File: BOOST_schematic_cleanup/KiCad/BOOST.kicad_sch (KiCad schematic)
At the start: 290 parts, among them J1 Conn_01x01_Pin, J10 Conn_02x15_2.54mm, J11 Conn_02x15_2.54mm, J2 Conn_01x01_Pin, J3 Conn_01x01_Pin, J4 Conn_01x01_Pin, J5 Conn_01x01_Pin, J6 Conn_01x01_Pin, J7 Conn_01x01_Pin, J8 Conn_01x01_Pin, J9 Conn_01x11, M1 HYG180N10, M10 HYG180N10, M2 HYG180N10, M3 HYG180N10, M4 HYG180N10, M5 HYG180N10, M6 HYG180N10, M7 HYG180N10, M8 HYG180N10, M9 HYG180N10, Q1 PNP, U1 L78L05_SOT89, U10 UCC21520DW, U101 74HC00, U102 74HC00, U103 74HC00, U104 74HC14, U105 74HC14, U106 CD74HC4066, U11 MCP6241, U12 MCP6241, U13 MCP6241, U14 MCP6561, U15 UCC21520DW, U16 LM2940_12, U17 L78L05_SOT89, U18 4017, U19 UCC21520DW, U2 MCP6561, U21 MCP6561, U22 MCP6241, U23 MCP6241, U24 MCP6241, U25 INA241A4xD, U26 MCP4451-103E/ST, U28 74HC4051, U3 MCP6241, U4 MCP6561, U5 MCP6561, U6 MCP6241, U7 MCP6241, U8 UCC21520DW

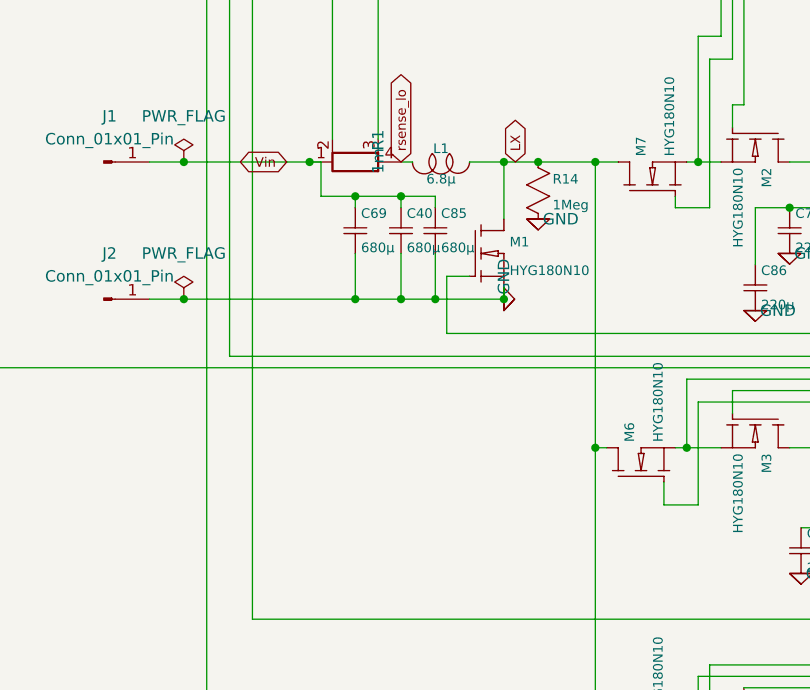
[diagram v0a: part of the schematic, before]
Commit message: added diodes from input to output
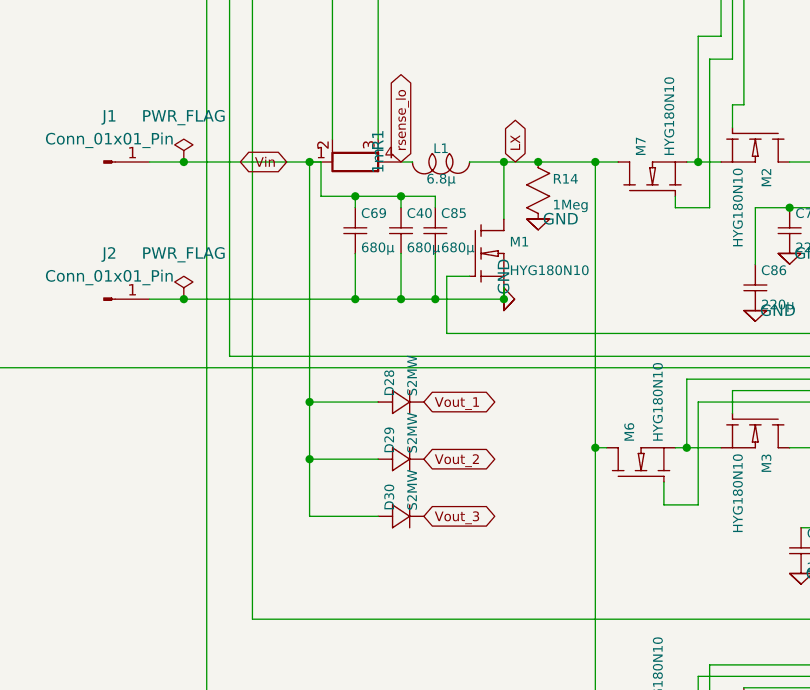
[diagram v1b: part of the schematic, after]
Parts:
- added D28, D29, D30: S2MW, Diode_SMD:D_SOD-123F, symbol ltspice:diode
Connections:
- net Vin: now also D28.2 (+), D29.2 (+), D30.2 (+)
- net Vout_1: now also D28.1 (-)
- net Vout_2: now also D29.1 (-)
- net Vout_3: now also D30.1 (-)

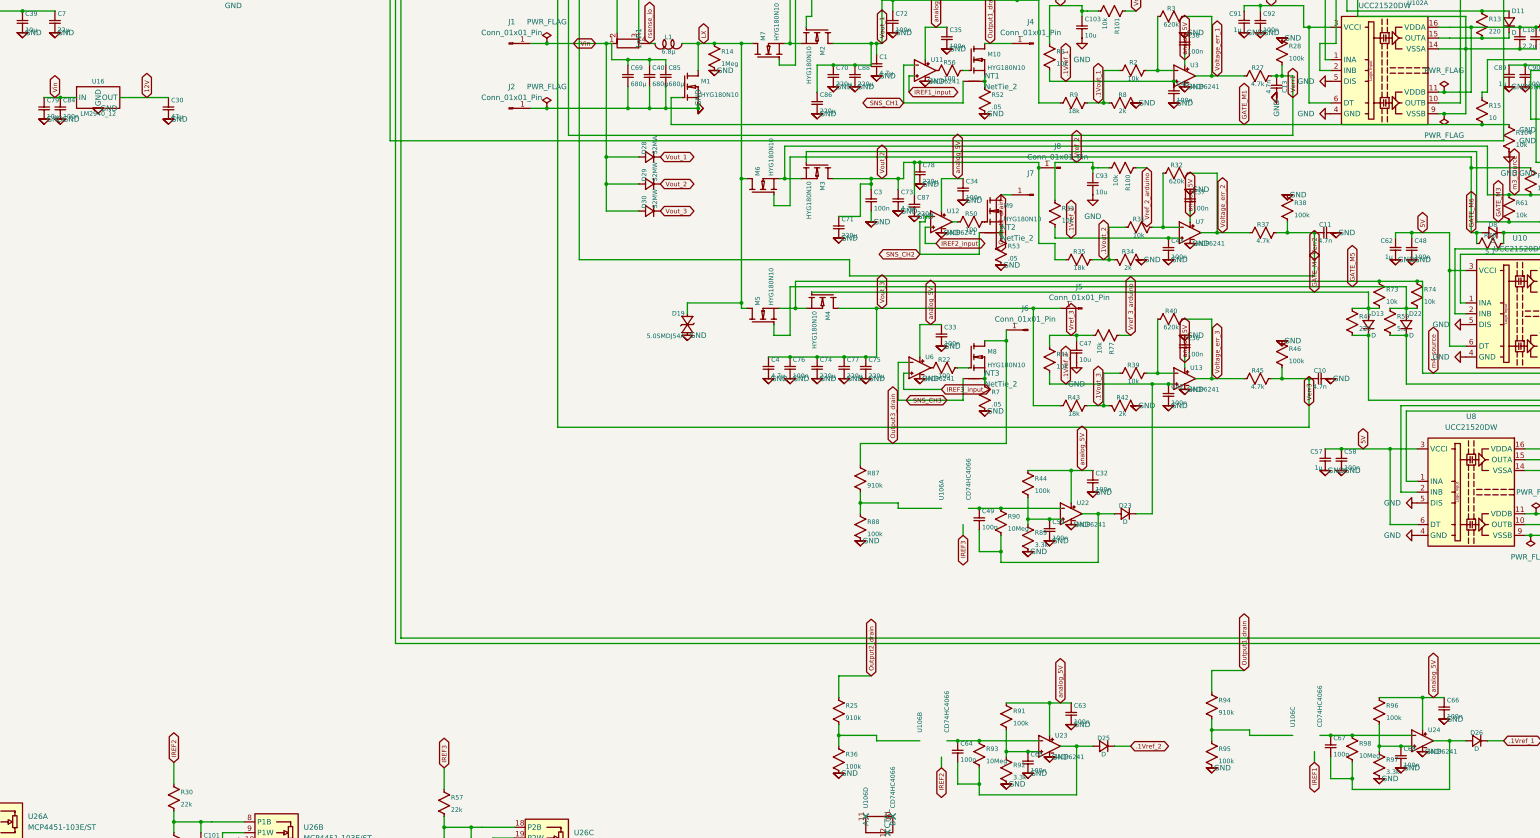
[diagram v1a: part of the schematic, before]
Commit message: changed power board to 6 layers
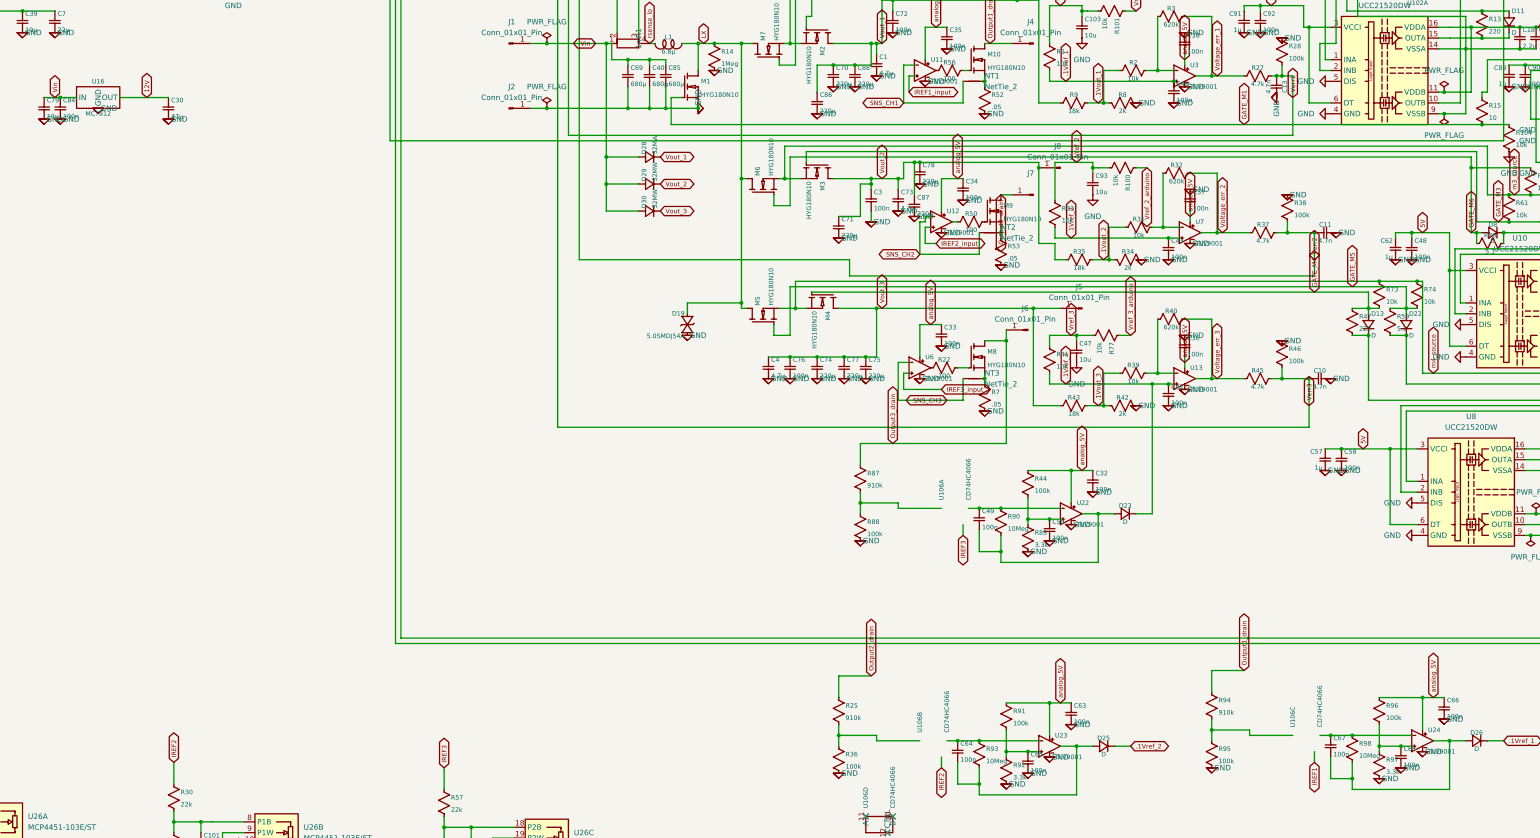
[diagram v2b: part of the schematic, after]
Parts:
- C70, C71, C75, C77, C78, C88: MPN EEH-ZU1H221P -> EEH-ZS1H221P
- U11, U12, U13, U22, U23, U24, U3, U6, U7: value MCP6241 -> TLV9001; MPN (none) -> TLV9001IDBVR
- U16: value LM2940_12 -> MC7812; MPN (none) -> MC7812BD2TR4G
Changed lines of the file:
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@@
 			)
 		)
-		(property "Value" "MCP6241"
+		(property "Value" "TLV9001"
 			(at 335.28 181.61 0)
 			(show_name no)
@@
 			)
 		)
-		(property "Sim.Library" "C:\\Users\\bubba\\AppData\\Local\\LTspice\\lib\\sub\\MCP6241.lib"
+		(property "Sim.Library" "../LTspice/TLV9001.lib"
 			(at 334.01 173.99 0)
 			(hide yes)
@@
 			)
 		)
+		(property "MPN" "TLV9001IDBVR"
+			(at 334.01 173.99 0)
+			(hide yes)
+			(show_name no)
+			(do_not_autoplace no)
+			(effects
+				(font
+					(size 1.27 1.27)
+				)
+			)
+		)
 		(pin "4"
 		)
@@
 			)
 		)
-		(property "MPN" "EEH-ZU1H221P"
+		(property "MPN" "EEH-ZS1H221P"
 			(at 248.92 139.7 0)
 			(hide yes)
@@
 			)
 		)
-		(property "MPN" "EEH-ZU1H221P"
+		(property "MPN" "EEH-ZS1H221P"
 			(at 256.54 208.28 0)
 			(hide yes)
@@
 			)
 		)
-		(property "Value" "MCP6241"
+		(property "Value" "TLV9001"
 			(at 273.05 143.51 0)
 			(show_name no)
@@
 			)
 		)
-		(property "Sim.Library" "C:\\Users\\bubba\\AppData\\Local\\LTspice\\lib\\sub\\MCP6241.lib"
+		(property "Sim.Library" "../LTspice/TLV9001.lib"
 			(at 271.78 135.89 0)
 			(hide yes)
@@
 			)
 		)
+		(property "MPN" "TLV9001IDBVR"
+			(at 271.78 135.89 0)
+			(hide yes)
+			(show_name no)
+			(do_not_autoplace no)
+			(effects
+				(font
+					(size 1.27 1.27)
+				)
+			)
+		)
 		(pin "3"
 		)
@@
 			)
 		)
-		(property "Value" "MCP6241"
+		(property "Value" "TLV9001"
 			(at 389.89 300.99 0)
 			(show_name no)
@@
 			)
 		)
-		(property "Sim.Library" "C:\\Users\\bubba\\AppData\\Local\\LTspice\\lib\\sub\\MCP6241.lib"
+		(property "Sim.Library" "../LTspice/TLV9001.lib"
 			(at 388.62 293.37 0)
 			(hide yes)
@@
 			)
 		)
+		(property "MPN" "TLV9001IDBVR"
+			(at 388.62 293.37 0)
+			(hide yes)
+			(show_name no)
+			(do_not_autoplace no)
+			(effects
+				(font
+					(size 1.27 1.27)
+				)
+			)
+		)
 		(pin "2"
 		)
@@
 			)
 		)
-		(property "Value" "MCP6241"
+		(property "Value" "TLV9001"
 			(at 271.78 213.36 0)
 			(show_name no)
@@
 			)
 		)
-		(property "Sim.Library" "C:\\Users\\bubba\\AppData\\Local\\LTspice\\lib\\sub\\MCP6241.lib"
+		(property "Sim.Library" "../LTspice/TLV9001.lib"
 			(at 270.51 205.74 0)
 			(hide yes)
@@
 			)
 		)
+		(property "MPN" "TLV9001IDBVR"
+			(at 270.51 205.74 0)
+			(hide yes)
+			(show_name no)
+			(do_not_autoplace no)
+			(effects
+				(font
+					(size 1.27 1.27)
+				)
+			)
+		)
 		(pin "2"
 		)
@@
 			)
 		)
-		(property "MPN" "EEH-ZU1H221P"
+		(property "MPN" "EEH-ZS1H221P"
 			(at 254 139.7 0)
 			(hide yes)
@@
 			)
 		)
-		(property "MPN" "EEH-ZU1H221P"
+		(property "MPN" "EEH-ZS1H221P"
 			(at 251.46 208.28 0)
 			(hide yes)
@@
 			)
 		)
-		(property "MPN" "EEH-ZU1H221P"
+		(property "MPN" "EEH-ZS1H221P"
 			(at 269.24 162.56 0)
 			(hide yes)
@@
 			)
 		)
-		(property "Value" "MCP6241"
+		(property "Value" "TLV9001"
 			(at 302.26 302.26 0)
 			(show_name no)
@@
 			)
 		)
-		(property "Sim.Library" "C:\\Users\\bubba\\AppData\\Local\\LTspice\\lib\\sub\\MCP6241.lib"
+		(property "Sim.Library" "../LTspice/TLV9001.lib"
 			(at 300.99 294.64 0)
 			(hide yes)
@@
 			)
 		)
+		(property "MPN" "TLV9001IDBVR"
+			(at 300.99 294.64 0)
+			(hide yes)
+			(show_name no)
+			(do_not_autoplace no)
+			(effects
+				(font
+					(size 1.27 1.27)
+				)
+			)
+		)
 		(pin "3"
 		)
@@
 			)
 		)
-		(property "Value" "MCP6241"
+		(property "Value" "TLV9001"
 			(at 334.01 215.9 0)
 			(show_name no)
@@
 			)
 		)
-		(property "Sim.Library" "C:\\Users\\bubba\\AppData\\Local\\LTspice\\lib\\sub\\MCP6241.lib"
+		(property "Sim.Library" "../LTspice/TLV9001.lib"
 			(at 332.74 208.28 0)
 			(hide yes)
@@
 			)
 		)
+		(property "MPN" "TLV9001IDBVR"
+			(at 332.74 208.28 0)
+			(hide yes)
+			(show_name no)
+			(do_not_autoplace no)
+			(effects
+				(font
+					(size 1.27 1.27)
+				)
+			)
+		)
 		(pin "1"
 		)
@@
 			)
 		)
-		(property "Value" "MCP6241"
+		(property "Value" "TLV9001"
 			(at 276.86 179.07 0)
 			(show_name no)
@@
 			)
 		)
-		(property "Sim.Library" "C:\\Users\\bubba\\AppData\\Local\\LTspice\\lib\\sub\\MCP6241.lib"
+		(property "Sim.Library" "../LTspice/TLV9001.lib"
 			(at 275.59 171.45 0)
 			(hide yes)
@@
 			)
 		)
+		(property "MPN" "TLV9001IDBVR"
+			(at 275.59 171.45 0)
+			(hide yes)
+			(show_name no)
+			(do_not_autoplace no)
+			(effects
+				(font
+					(size 1.27 1.27)
+				)
+			)
+		)
 		(pin "4"
 		)
@@
 			)
 		)
-		(property "Value" "LM2940_12"
+		(property "Value" "MC7812"
 			(at 77.47 150.495 0)
 			(show_name no)
@@
 			)
 		)
-		(property "Sim.Library" "LM2940_12.lib"
+		(property "Sim.Library" "../LTspice/MC7812.lib"
 			(at 77.47 147.32 0)
 			(hide yes)
@@
 			)
 		)
-		(property "Sim.Name" "LM2940_12"
+		(property "Sim.Name" "MC7812_TYP"
 			(at 77.47 147.32 0)
 			(hide yes)
@@
 			)
 		)
+		(property "MPN" "MC7812BD2TR4G"
+			(at 77.47 147.32 0)
+			(hide yes)
+			(show_name no)
+			(do_not_autoplace no)
+			(effects
+				(font
+					(size 1.27 1.27)
+				)
+			)
+		)
 		(pin "2"
 		)
@@
 			)
 		)
-		(property "Value" "MCP6241"
+		(property "Value" "TLV9001"
 			(at 307.34 247.65 0)
 			(show_name no)
@@
 			)
 		)
-		(property "Sim.Library" "C:\\Users\\bubba\\AppData\\Local\\LTspice\\lib\\sub\\MCP6241.lib"
+		(property "Sim.Library" "../LTspice/TLV9001.lib"
 			(at 306.07 240.03 0)
 			(hide yes)
@@
 			)
 		)
+		(property "MPN" "TLV9001IDBVR"
+			(at 306.07 240.03 0)
+			(hide yes)
+			(show_name no)
+			(do_not_autoplace no)
+			(effects
+				(font
+					(size 1.27 1.27)
+				)
+			)
+		)
 		(pin "2"
 		)
@@
 			)
 		)
-		(property "MPN" "EEH-ZU1H221P"
+		(property "MPN" "EEH-ZS1H221P"
 			(at 250.19 175.26 0)
 			(hide yes)
@@
 			)
 		)
-		(property "Value" "MCP6241"
+		(property "Value" "TLV9001"
 			(at 334.01 144.78 0)
 			(show_name no)
@@
 			)
 		)
-		(property "Sim.Library" "C:\\Users\\bubba\\AppData\\Local\\LTspice\\lib\\sub\\MCP6241.lib"
+		(property "Sim.Library" "../LTspice/TLV9001.lib"
 			(at 332.74 137.16 0)
 			(hide yes)
@@
 			(at 332.74 137.16 0)
 			(hide yes)
+			(show_name no)
+			(do_not_autoplace no)
+			(effects
+				(font
+					(size 1.27 1.27)
+				)
+			)
+		)
+		(property "MPN" "TLV9001IDBVR"
+			(at 332.74 137.16 0)
+			(hide yes)
